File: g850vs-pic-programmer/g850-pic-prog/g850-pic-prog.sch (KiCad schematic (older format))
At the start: 30 parts, among them J1 Conn_01x11_Male, Q1 BC547, Q2 2N3906, Q3 BC547, U1 74HC14, U2 PIC16F84-XXP

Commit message: Updated values on PIC programmer to get one of my PCBs working. Capacitor values don't seem to be correct on original circuit.
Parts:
- C1, C3, C4: value 680pF -> 10nF
- C2: value 680pF -> n27 or 10n
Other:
- note added: "Values different to original circuit.\nThese values work."
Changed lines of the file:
@@
 P 2750 3550
 F 0 "C2" H 2842 3596 50  0000 L CNN
-F 1 "680pF" H 2842 3505 50  0000 L CNN
+F 1 "n27 or 10n" H 2842 3505 50  0000 L CNN
 F 2 "Capacitor_THT:C_Axial_L5.1mm_D3.1mm_P7.50mm_Horizontal" H 2750 3550 50  0001 C CNN
 F 3 "~" H 2750 3550 50  0001 C CNN
@@
 P 2650 2350
 F 0 "C1" H 2742 2396 50  0000 L CNN
-F 1 "680pF" H 2742 2305 50  0000 L CNN
+F 1 "10nF" H 2742 2305 50  0000 L CNN
 F 2 "Capacitor_THT:C_Axial_L5.1mm_D3.1mm_P7.50mm_Horizontal" H 2650 2350 50  0001 C CNN
 F 3 "~" H 2650 2350 50  0001 C CNN
@@
 P 3500 2350
 F 0 "C3" H 3592 2396 50  0000 L CNN
-F 1 "680pF" H 3592 2305 50  0000 L CNN
+F 1 "10nF" H 3592 2305 50  0000 L CNN
 F 2 "Capacitor_THT:C_Axial_L5.1mm_D3.1mm_P7.50mm_Horizontal" H 3500 2350 50  0001 C CNN
 F 3 "~" H 3500 2350 50  0001 C CNN
@@
 P 4700 2350
 F 0 "C4" H 4792 2396 50  0000 L CNN
-F 1 "680pF" H 4792 2305 50  0000 L CNN
+F 1 "10nF" H 4792 2305 50  0000 L CNN
 F 2 "Capacitor_THT:C_Axial_L5.1mm_D3.1mm_P7.50mm_Horizontal" H 4700 2350 50  0001 C CNN
 F 3 "~" H 4700 2350 50  0001 C CNN
@@
 Text GLabel 4450 4600 2    50   Input ~ 0
 V+
+Text Notes 1350 4550 0    50   ~ 0
+Values different to original circuit.\nThese values work.
 $EndSCHEMATC

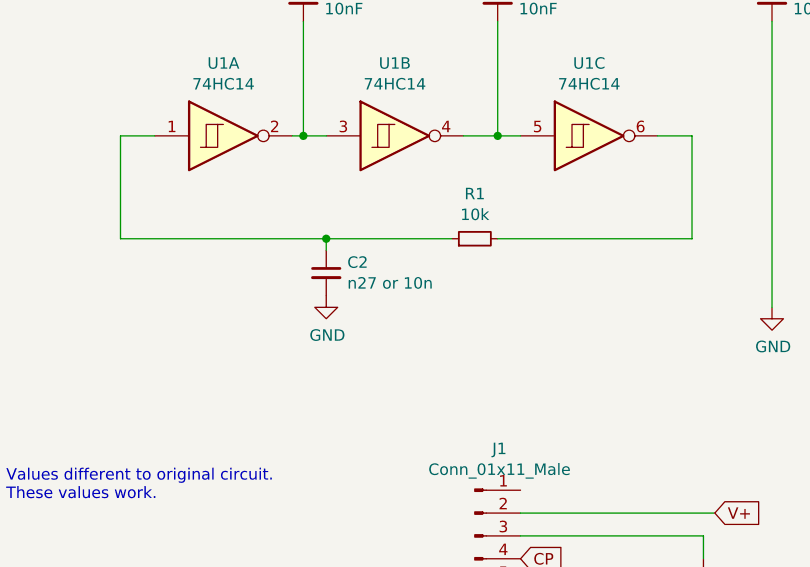
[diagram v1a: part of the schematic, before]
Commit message: C2 should be n27, or 270pF. 10nF does not work.
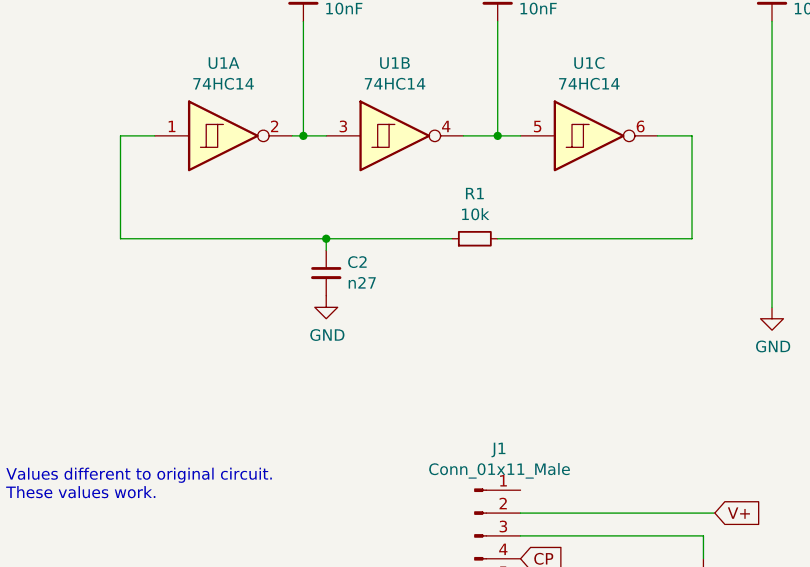
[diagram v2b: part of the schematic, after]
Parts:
- C2: value n27 or 10n -> n27
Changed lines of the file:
@@
 P 2750 3550
 F 0 "C2" H 2842 3596 50  0000 L CNN
-F 1 "n27 or 10n" H 2842 3505 50  0000 L CNN
+F 1 "n27" H 2842 3505 50  0000 L CNN
 F 2 "Capacitor_THT:C_Axial_L5.1mm_D3.1mm_P7.50mm_Horizontal" H 2750 3550 50  0001 C CNN
 F 3 "~" H 2750 3550 50  0001 C CNN

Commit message: Updates
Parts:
- Q1, Q3: symbol Microtan_65_CPU-cache:BC547 -> g850-pic-prog-rescue:BC547-Microtan_65_CPU-cache
- Q2: symbol Microtan_exp:2N3906 -> g850-pic-prog-rescue:2N3906-Microtan_exp
- U2: footprint Package_DIP:DIP-18_W7.62mm -> Socket:DIP_Socket-18_W4.3_W5.08_W7.62_W10.16_W10.9_3M_218-3341-00-0602J
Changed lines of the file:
@@
 F 0 "U2" H 7400 4731 50  0000 C CNN
 F 1 "PIC16F84-XXP" H 7400 4640 50  0000 C CNN
-F 2 "Package_DIP:DIP-18_W7.62mm" H 7400 3650 50  0001 C CIN
+F 2 "Socket:DIP_Socket-18_W4.3_W5.08_W7.62_W10.16_W10.9_3M_218-3341-00-0602J" H 7400 3650 50  0001 C CIN
 F 3 "http://ww1.microchip.com/downloads/en/DeviceDoc/30430c.pdf" H 7400 3650 50  0001 C CNN
 	1    7400 3650
@@
 	9700 5750 9950 5750
 $Comp
-L Microtan_65_CPU-cache:BC547 Q3
+L g850-pic-prog-rescue:BC547-Microtan_65_CPU-cache Q3
 U 1 1 5F21B5D1
 P 9800 2800
@@
 $EndComp
 $Comp
-L Microtan_65_CPU-cache:BC547 Q1
+L g850-pic-prog-rescue:BC547-Microtan_65_CPU-cache Q1
 U 1 1 5F197F3A
 P 9150 5750
@@
 	1500 6600 1500 6800
 $Comp
-L Microtan_exp:2N3906 Q2
+L g850-pic-prog-rescue:2N3906-Microtan_exp Q2
 U 1 1 5F336922
 P 9700 1150
@@
 $EndComp
 $Comp
-L power:GND #PWR?
+L power:GND #PWR0119
 U 1 1 5F35D117
 P 4400 4800
-F 0 "#PWR?" H 4400 4550 50  0001 C CNN
+F 0 "#PWR0119" H 4400 4550 50  0001 C CNN
 F 1 "GND" H 4405 4627 50  0000 C CNN
 F 2 "" H 4400 4800 50  0001 C CNN
